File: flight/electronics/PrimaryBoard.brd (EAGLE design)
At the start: 79 x 80.3 mm, 10 parts

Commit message: primary board updates
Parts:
- added U$3, U$4, U$5, U$6: (no value), holes:3,0
- moved POWER_BOARD 21.1 mm to (91.0, 65.0)
- moved ARDUCAM-A 20.1 mm to (37.6, 89.4)
- moved ARDUCAM-B 20.1 mm to (15.1, 89.4)
- moved SENSOR_BOARD 20.1 mm to (60.0, 89.4)
- moved U$1 18.0 mm to (15.0, 63.0)
- moved ESP32 15.0 mm to (74.1, 27.1)
- moved R1 12.2 mm to (73.0, 65.0)
- moved R2 12.2 mm to (73.0, 62.0)
- moved U$2 9.49 mm to (25.0, 19.0)
- moved PIEZO 8.00 mm to (47.0, 9.00)
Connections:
- net +5V: no longer ESP32.30
- net VBAT: now also ESP32.30
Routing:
- net GND: track 223.2 -> 0.00 mm
- net VBAT: track 3.92 -> 101.5 mm
- net HSPI_MOSI: track 84.8 -> 115.7 mm
- net HSPI_MISO: track 83.2 -> 113.4 mm
- net MOSI_CLK: track 81.9 -> 111.2 mm
- net I2C_SCL: track 93.5 -> 121.7 mm
- net I2C_SDA: track 104.0 -> 131.7 mm
- net VSPI_MOSI: track 143.0 -> 166.8 mm
- net VSPI_CLK: track 113.8 -> 137.6 mm
- net VSPI_MISO: track 114.2 -> 138.0 mm
- net ARDUCAM-A_CS: track 109.4 -> 133.2 mm
- net SD_CS: track 61.8 -> 83.5 mm
- net +3V3: track 157.8 -> 177.2 mm
- net ARDUCAM-B_CS: track 114.1 -> 132.3 mm
- net GPIO2: track 39.9 -> 57.3 mm
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- added copper zone on layer 1, net GND
- added copper zone on layer 16, net GND
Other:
- board size 79 x 80.3 mm -> 100 x 100 mm
- board text added: "ARUDCAM A"
- board text added: "ARUDCAM B"
- board text added: "BUZZER"
- board text added: "ESP32 DEVBOARD"
- board text added: "KAOS-1 PRIMARY BOARD REV1"
- board text added: "POWER BOARD"
- board text added: "SENSOR BOARD"

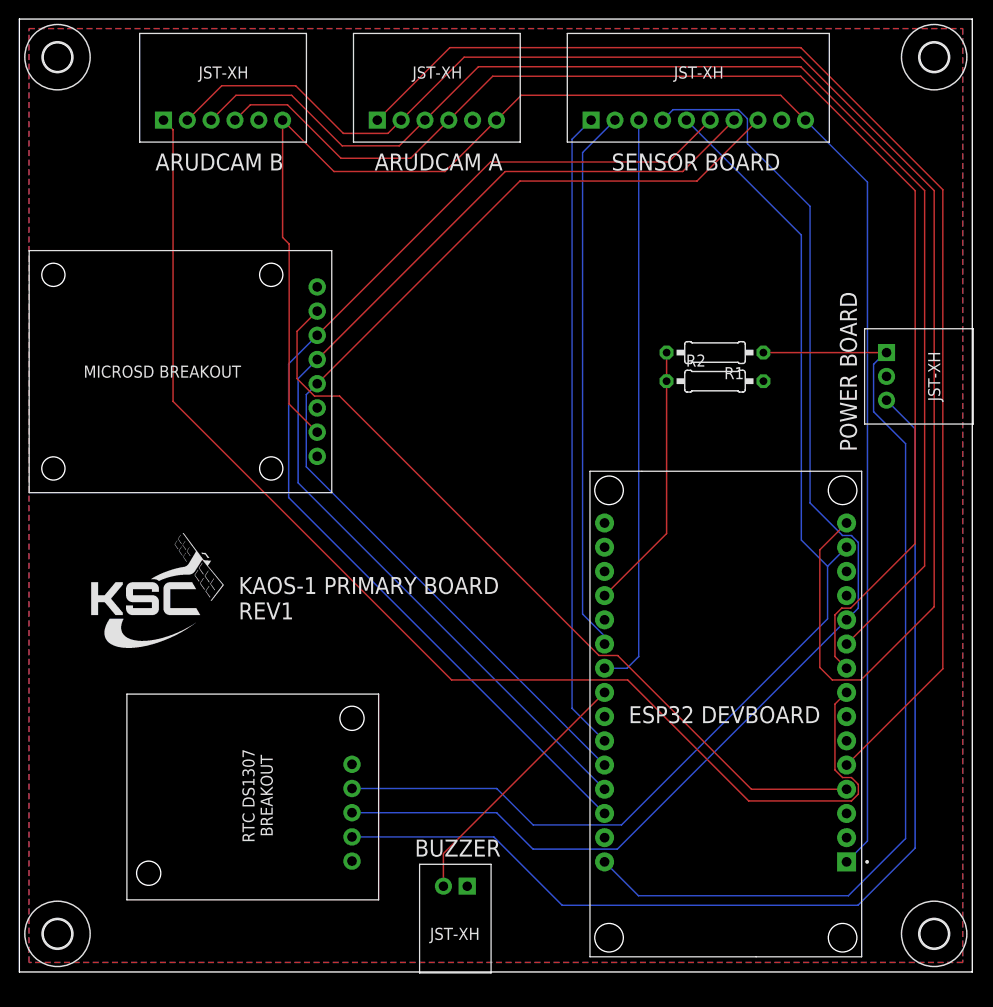
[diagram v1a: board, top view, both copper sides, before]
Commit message: round board corners
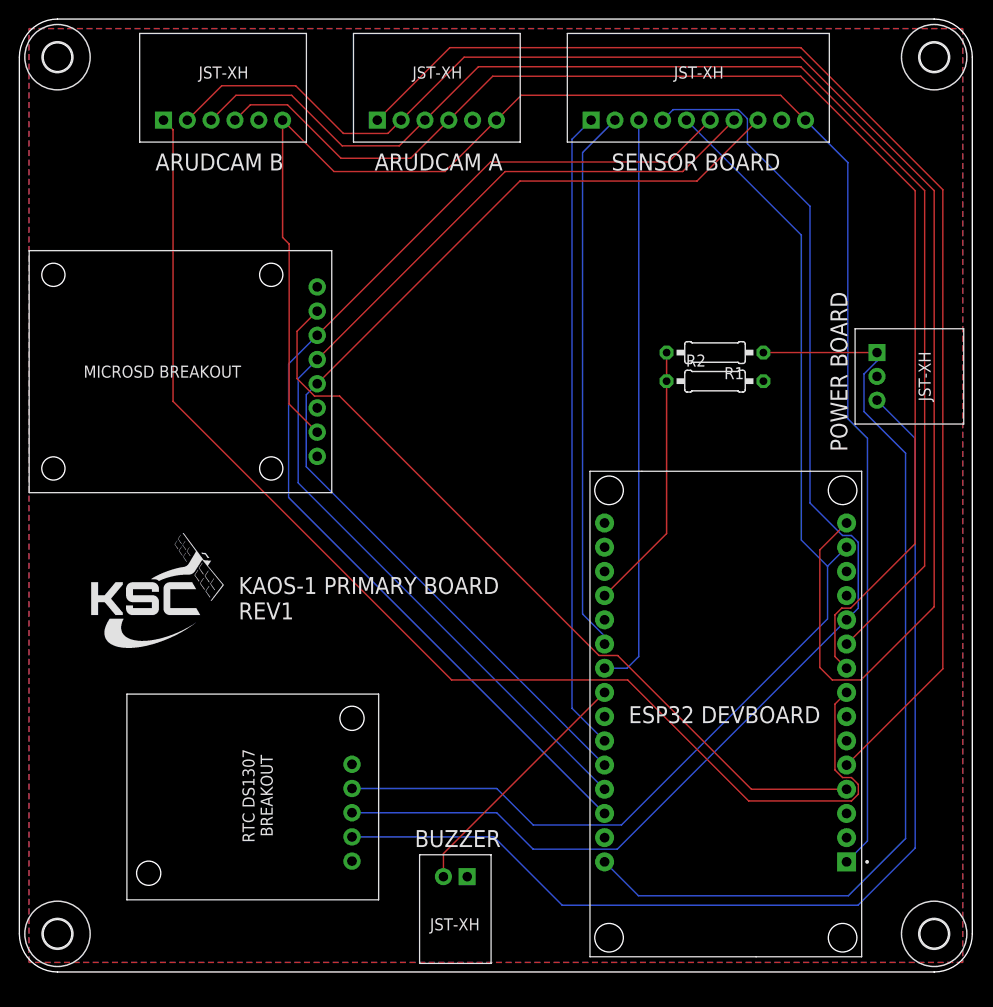
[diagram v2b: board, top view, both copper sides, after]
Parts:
- moved PIEZO 1.00 mm to (47.0, 10.0)
- moved POWER_BOARD 1.00 mm to (90.0, 65.0)
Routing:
- net PIEZO: track 27.3 -> 26.3 mm
- net VBAT: track 101.5 -> 100.8 mm
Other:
- outline, holes or cut-outs redrawn
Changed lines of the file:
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@@
 <board>
 <plain>
-<wire x1="0" y1="0" x2="100" y2="0" width="0" layer="20"/>
-<wire x1="100" y1="0" x2="100" y2="100" width="0" layer="20"/>
-<wire x1="100" y1="100" x2="0" y2="100" width="0" layer="20"/>
-<wire x1="0" y1="100" x2="0" y2="0" width="0" layer="20"/>
+<wire x1="4" y1="0" x2="96" y2="0" width="0" layer="20"/>
+<wire x1="100" y1="4" x2="100" y2="96" width="0" layer="20"/>
+<wire x1="96" y1="100" x2="4" y2="100" width="0" layer="20"/>
 <text x="74" y="27" size="1.778" layer="21" font="vector" align="center">ESP32 DEVBOARD</text>
 <text x="21" y="85" size="1.778" layer="21" font="vector" align="center">ARUDCAM B</text>
 <text x="44" y="85" size="1.778" layer="21" font="vector" align="center">ARUDCAM A</text>
 <text x="71" y="85" size="1.778" layer="21" font="vector" align="center">SENSOR BOARD</text>
-<text x="46" y="13" size="1.778" layer="21" font="vector" align="center">BUZZER</text>
-<text x="87" y="63" size="1.778" layer="21" font="vector" rot="R90" align="center">POWER BOARD</text>
+<text x="46" y="14" size="1.778" layer="21" font="vector" align="center">BUZZER</text>
+<text x="86" y="63" size="1.778" layer="21" font="vector" rot="R90" align="center">POWER BOARD</text>
 <text x="23" y="37" size="1.778" layer="21" font="vector">KAOS-1 PRIMARY BOARD
 REV1</text>
@@
 <rectangle x1="17.1577" y1="46.0121" x2="17.2593" y2="46.0375" layer="21"/>
 <rectangle x1="17.1323" y1="46.0375" x2="17.2593" y2="46.0629" layer="21"/>
+<wire x1="0" y1="96" x2="0" y2="4" width="0" layer="20"/>
+<wire x1="4" y1="0" x2="0" y2="4" width="0" layer="20" curve="-90"/>
+<wire x1="0" y1="96" x2="4" y2="100" width="0" layer="20" curve="-90"/>
+<wire x1="96" y1="100" x2="100" y2="96" width="0" layer="20" curve="-90"/>
+<wire x1="96" y1="0" x2="100" y2="4" width="0" layer="20" curve="90"/>
 </plain>
 <attributes>
@@
 <element name="ARDUCAM-A" library="Rembrandt Electronics - JST XH Connectors v1-0" package="JST-XH_S6B" value="JST-XH-06-PIN" x="37.5615" y="89.39" smashed="yes"/>
 <element name="U$1" library="Breakouts" package="MICROSDBREAKOUT5V" value="MICROSDBREAKOUT5V" x="15" y="63" smashed="yes"/>
-<element name="POWER_BOARD" library="Rembrandt Electronics - JST XH Connectors v1-0" package="JST-XH_S3B" value="JST-XH-03-PIN" x="91" y="65" smashed="yes" rot="R270"/>
+<element name="POWER_BOARD" library="Rembrandt Electronics - JST XH Connectors v1-0" package="JST-XH_S3B" value="JST-XH-03-PIN" x="90" y="65" smashed="yes" rot="R270"/>
 <element name="U$2" library="Breakouts" package="DS1307BREAKOUT" value="DS1307BREAKOUT" x="25" y="19" smashed="yes" rot="R90"/>
 <element name="R1" library="rcl" library_urn="urn:adsk.eagle:library:334" package="0207/10" package3d_urn="urn:adsk.eagle:package:23491/2" value="2000" x="73" y="65" smashed="yes" rot="R180">
@@
 <attribute name="VALUE" x="70.7394" y="61.365" size="1.27" layer="27" ratio="10"/>
 </element>
-<element name="PIEZO" library="Rembrandt Electronics - JST XH Connectors v1-0" package="JST-XH_S2B" value="JST-XH-02-PIN" x="47" y="9" smashed="yes" rot="R180"/>
+<element name="PIEZO" library="Rembrandt Electronics - JST XH Connectors v1-0" package="JST-XH_S2B" value="JST-XH-02-PIN" x="47" y="10" smashed="yes" rot="R180"/>
 <element name="ARDUCAM-B" library="Rembrandt Electronics - JST XH Connectors v1-0" package="JST-XH_S6B" value="JST-XH-06-PIN" x="15.123" y="89.39" smashed="yes"/>
 <element name="SENSOR_BOARD" library="Rembrandt Electronics - JST XH Connectors v1-0" package="JST-XH_S10B" value="JST-XH-10-PIN" x="60" y="89.39" smashed="yes"/>
@@
 <contactref element="POWER_BOARD" pad="PIN3"/>
 <contactref element="U$2" pad="5V"/>
-<wire x1="91" y1="60" x2="94" y2="57" width="0.1524" layer="16"/>
-<wire x1="94" y1="57" x2="94" y2="13" width="0.1524" layer="16"/>
+<wire x1="90" y1="60" x2="94" y2="56" width="0.1524" layer="16"/>
+<wire x1="94" y1="56" x2="94" y2="13" width="0.1524" layer="16"/>
 <wire x1="94" y1="13" x2="88" y2="7" width="0.1524" layer="16"/>
 <wire x1="88" y1="7" x2="56.965" y2="7" width="0.1524" layer="16"/>
@@
 <contactref element="POWER_BOARD" pad="PIN1"/>
 <contactref element="R1" pad="1"/>
-<wire x1="91" y1="65" x2="78.08" y2="65" width="0.1524" layer="1"/>
+<wire x1="90" y1="65" x2="78.08" y2="65" width="0.1524" layer="1"/>
 <contactref element="ESP32" pad="30"/>
 <wire x1="61.41" y1="11.555" x2="64.965" y2="8" width="0.1524" layer="16"/>
 <wire x1="87" y1="8" x2="93" y2="14" width="0.1524" layer="16"/>
-<wire x1="93" y1="14" x2="93" y2="55.4398375" width="0.1524" layer="16"/>
-<wire x1="93" y1="55.4398375" x2="89.6428" y2="58.7970375" width="0.1524" layer="16"/>
-<wire x1="90.873" y1="65" x2="89.6428" y2="63.7698" width="0.1524" layer="16"/>
-<wire x1="90.873" y1="65" x2="91" y2="65" width="0.1524" layer="16"/>
+<wire x1="93" y1="14" x2="93" y2="54.4398375" width="0.1524" layer="16"/>
+<wire x1="93" y1="54.4398375" x2="88.6428" y2="58.7970375" width="0.1524" layer="16"/>
+<wire x1="90" y1="64.127" x2="88.6428" y2="62.7698" width="0.1524" layer="16"/>
+<wire x1="90" y1="64.127" x2="90" y2="65" width="0.1524" layer="16"/>
 <wire x1="64.965" y1="8" x2="87" y2="8" width="0.1524" layer="16"/>
-<wire x1="89.6428" y1="58.7970375" x2="89.6428" y2="63.7698" width="0.1524" layer="16"/>
+<wire x1="88.6428" y1="58.7970375" x2="88.6428" y2="62.7698" width="0.1524" layer="16"/>
 </signal>
 <signal name="BAT_MEASURE">
@@
 <wire x1="82.5" y1="89.39" x2="79.89" y2="92" width="0.1524" layer="1"/>
 <wire x1="79.89" y1="92" x2="52.6715" y2="92" width="0.1524" layer="1"/>
-<wire x1="89" y1="13.745" x2="86.81" y2="11.555" width="0.1524" layer="16"/>
+<wire x1="86.81" y1="11.555" x2="89" y2="13.745" width="0.1524" layer="16"/>
 <wire x1="33.013" y1="84" x2="27.623" y2="89.39" width="0.1524" layer="1"/>
 <wire x1="50.0615" y1="89.39" x2="44.6715" y2="84" width="0.1524" layer="1"/>
 <wire x1="44.6715" y1="84" x2="33.013" y2="84" width="0.1524" layer="1"/>
-<wire x1="89" y1="82.89" x2="89" y2="13.745" width="0.1524" layer="16"/>
-<wire x1="82.5" y1="89.39" x2="89" y2="82.89" width="0.1524" layer="16"/>
+<wire x1="82.5" y1="89.39" x2="86.945" y2="84.945" width="0.1524" layer="16"/>
 <wire x1="27.623" y1="89.39" x2="27.623" y2="77.08181875" width="0.1524" layer="1"/>
 <wire x1="27.623" y1="77.08181875" x2="28.3064" y2="76.39841875" width="0.1524" layer="1"/>
 <wire x1="28.3064" y1="76.39841875" x2="28.3064" y2="59.5996" width="0.1524" layer="1"/>
 <wire x1="28.3064" y1="59.5996" x2="31.256" y2="56.65" width="0.1524" layer="1"/>
+<wire x1="89" y1="13.745" x2="89" y2="56" width="0.1524" layer="16"/>
+<wire x1="86.945" y1="58.055" x2="86.945" y2="84.945" width="0.1524" layer="16"/>
+<wire x1="89" y1="56" x2="86.945" y2="58.055" width="0.1524" layer="16"/>
 </signal>
 <signal name="MOSI_CLK">
@@
 <contactref element="PIEZO" pad="PIN2"/>
 <contactref element="ESP32" pad="23"/>
-<wire x1="44.5" y1="9" x2="44.5" y2="12.425" width="0.1524" layer="1"/>
+<wire x1="44.5" y1="10" x2="44.5" y2="12.425" width="0.1524" layer="1"/>
 <wire x1="44.5" y1="12.425" x2="61.41" y2="29.335" width="0.1524" layer="1"/>
 </signal>

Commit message: shrink primary to 90mm
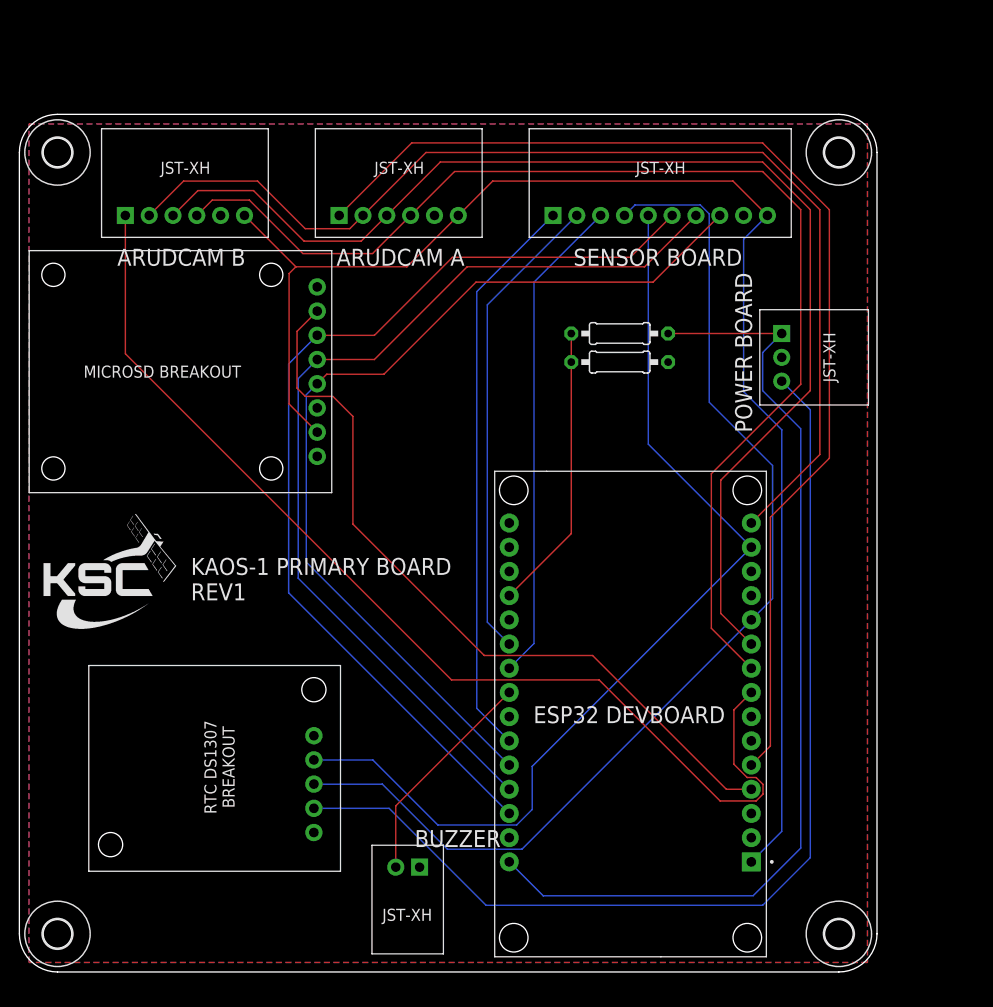
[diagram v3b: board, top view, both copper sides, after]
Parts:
- R1: value 2000 -> 2kΩ
- R2: value 1000 -> 1kΩ
- moved U$4 14.1 mm to (86.0, 86.0)
- moved ARDUCAM-A 10.8 mm to (33.6, 79.4)
- moved ARDUCAM-B 10.8 mm to (11.1, 79.4)
- moved SENSOR_BOARD 10.8 mm to (56.0, 79.4)
- moved POWER_BOARD 10.2 mm to (80.0, 67.0)
- moved R1 10.2 mm to (63.0, 67.0)
- moved R2 10.2 mm to (63.0, 64.0)
- moved ESP32 10.0 mm to (64.1, 27.1)
- moved U$3 10.0 mm to (86.0, 4.00)
- moved U$5 10.0 mm to (4.00, 86.0)
- moved PIEZO 5.10 mm to (42.0, 11.0)
- moved U$2 5.00 mm to (21.0, 22.0)
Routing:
- net VSPI_MOSI: track 166.8 -> 115.6 mm
- net +3V3: track 177.2 -> 153.1 mm
- net I2C_SCL: track 121.7 -> 102.7 mm
- net ARDUCAM-B_CS: track 132.3 -> 114.4 mm
- net I2C_SDA: track 131.7 -> 114.7 mm
- net ARDUCAM-A_CS: track 133.2 -> 119.2 mm
- net MOSI_CLK: track 111.2 -> 98.9 mm
- net HSPI_MISO: track 113.4 -> 101.1 mm
- net HSPI_MOSI: track 115.7 -> 103.5 mm
- net VSPI_CLK: track 137.6 -> 125.3 mm
- net VSPI_MISO: track 138.0 -> 126.5 mm
- net GPIO3: track 60.4 -> 51.5 mm
- net GPIO2: track 57.3 -> 49.8 mm
- net GPIO1: track 67.4 -> 59.9 mm
- net +5V: track 113.2 -> 109.6 mm
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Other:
- board size 100 x 100 mm -> 90 x 90 mm

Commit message: primary board redesign
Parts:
- removed SENSOR_BOARD: JST-XH-10-PIN, Rembrandt Electronics - JST XH Connectors v1-0:JST-XH_S10B
- removed U$3, U$4, U$5, U$6: (no value), holes:3,0
- added H1, H2, H3, H4: MOUNT-PAD-ROUND3.0, holes:3,0-PAD
- added X1: JST-XH-07-PIN, Rembrandt Electronics - JST XH Connectors v1-0:JST-XH_S7B
- U$2: value DS1307BREAKOUT -> PCF8523BREAKOUT; device Breakouts:DS1307BREAKOUT -> Breakouts:PCF8523BREAKOUT
- moved U$1 13.0 mm to (15.0, 50.0)
- moved R1 12.5 mm to (52.0, 61.0)
- moved R2 12.5 mm to (52.0, 58.0)
- moved POWER_BOARD 11.2 mm to (70.0, 62.0)
- moved ESP32 10.0 mm to (54.1, 27.1)
- moved ARDUCAM-A 9.06 mm to (32.5, 70.4)
- moved ARDUCAM-B 9.00 mm to (11.0, 70.4)
- moved PIEZO 7.07 mm to (35.0, 10.0)
- moved U$2 6.40 mm to (16.0, 26.0)
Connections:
- removed net +5V: POWER_BOARD.PIN3, U$2.5V
- removed net MOSI_CLK: ESP32.26, SENSOR_BOARD.PIN8, U$1.CLK
- new net HSPI_CLK: ESP32.26, U$1.CLK
- net +3V3: now also POWER_BOARD.PIN2, U$2.VCC, X1.PIN2; no longer SENSOR_BOARD.PIN10
- net GND: now also H1.B3,0, H2.B3,0, H3.B3,0, H4.B3,0, POWER_BOARD.PIN1, X1.PIN1; no longer POWER_BOARD.PIN2, SENSOR_BOARD.PIN9
- net GPIO1: now also X1.PIN5; no longer SENSOR_BOARD.PIN1
- net GPIO2: now also X1.PIN6; no longer SENSOR_BOARD.PIN2
- net GPIO3: now also X1.PIN7; no longer SENSOR_BOARD.PIN3
- net HSPI_MISO: no longer SENSOR_BOARD.PIN7
- net HSPI_MOSI: no longer SENSOR_BOARD.PIN6
- net I2C_SCL: now also X1.PIN3; no longer SENSOR_BOARD.PIN5
- net I2C_SDA: now also X1.PIN4; no longer SENSOR_BOARD.PIN4
- net SD_CS: now also ESP32.3; no longer ESP32.4
- net VBAT: now also POWER_BOARD.PIN3; no longer ESP32.30, POWER_BOARD.PIN1
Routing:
- net +5V: track 109.6 -> 0.00 mm
- net +3V3: track 153.1 -> 256.2 mm
- net MOSI_CLK: track 98.9 -> 0.00 mm
- net VBAT: track 102.5 -> 14.6 mm
- net HSPI_MISO: track 101.1 -> 38.5 mm
- net HSPI_MOSI: track 103.5 -> 43.8 mm
- net VSPI_MOSI: track 115.6 -> 67.1 mm
- net VSPI_MISO: track 126.5 -> 82.7 mm
- net VSPI_CLK: track 125.3 -> 84.1 mm
- net HSPI_CLK: track 0.00 -> 33.0 mm
- net ARDUCAM-A_CS: track 119.2 -> 95.9 mm
- net I2C_SDA: track 114.7 -> 95.8 mm
- net SD_CS: track 80.7 -> 67.0 mm
- net I2C_SCL: track 102.7 -> 92.3 mm
- net BAT_MEASURE: track 30.2 -> 23.8 mm
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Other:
- board size 90 x 90 mm -> 80 x 80 mm

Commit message: final touches
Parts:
- moved POWER_BOARD 67.2 mm to (27.5, 10.0), turned to 180 degrees
- moved R1 10.0 mm to (42.0, 62.0), turned to 0 degrees
- moved R2 10.0 mm to (42.0, 59.0), turned to 180 degrees
- moved PIEZO 1.00 mm to (36.0, 10.0)
- moved U$1 1.00 mm to (15.0, 51.0)
- moved U$2 1.00 mm to (16.0, 27.0)
- moved ESP32 0.13 mm to (54.0, 27.0)
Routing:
- net +3V3: track 256.2 -> 156.3 mm, vias 0 -> 1
- net VBAT: track 14.6 -> 61.4 mm
- net ARDUCAM-B_CS: track 112.0 -> 108.5 mm, vias 1 -> 0
- net VSPI_CLK: track 84.1 -> 85.4 mm
- net BAT_MEASURE: track 23.8 -> 25.0 mm
- net SD_CS: track 67.0 -> 67.9 mm
- net HSPI_MISO: track 38.5 -> 39.4 mm
- net HSPI_MOSI: track 43.8 -> 44.8 mm
- net HSPI_CLK: track 33.0 -> 33.9 mm
- net GPIO1: track 65.3 -> 66.1 mm
- net VSPI_MISO: track 82.7 -> 83.4 mm
- net PIEZO: track 23.0 -> 22.5 mm
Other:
- board text added: "POWER"
- board text removed: "POWER BOARD"

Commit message: final board tweaks
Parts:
- removed POWER_BOARD: JST-XH-03-PIN, Rembrandt Electronics - JST XH Connectors v1-0:JST-XH_S3B
- added X2: JST-XH-03-PIN, JST-XH Connectors:JST-XH_S3B
- ARDUCAM-A, ARDUCAM-B: device Rembrandt Electronics - JST XH Connectors v1-0:JST-XH_S6B -> JST-XH Connectors:JST-XH_S6B
- PIEZO: device Rembrandt Electronics - JST XH Connectors v1-0:JST-XH_S2B -> JST-XH Connectors:JST-XH_S2B
- X1: device Rembrandt Electronics - JST XH Connectors v1-0:JST-XH_S7B -> JST-XH Connectors:JST-XH_S7B
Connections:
- net +3V3: now also X2.PIN2; no longer POWER_BOARD.PIN2
- net GND: now also X2.PIN1; no longer POWER_BOARD.PIN1
- net VBAT: now also X2.PIN3; no longer POWER_BOARD.PIN3
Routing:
- net I2C_SDA: track 95.8 -> 96.5 mm
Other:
- board text added: "ARDUCAM A"
- board text added: "ARDUCAM B"
- board text removed: "ARUDCAM A"
- board text removed: "ARUDCAM B"
